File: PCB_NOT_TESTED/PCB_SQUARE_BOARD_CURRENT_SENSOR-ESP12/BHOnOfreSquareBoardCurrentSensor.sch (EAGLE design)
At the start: 26 parts, among them J6 8p, J7 8p, K1 OMRON-G3MB-202P-SSR2, K2 OMRON-G3MB-202P-SSR2, Q1 S8050, U2 esp12, X2 PLUG

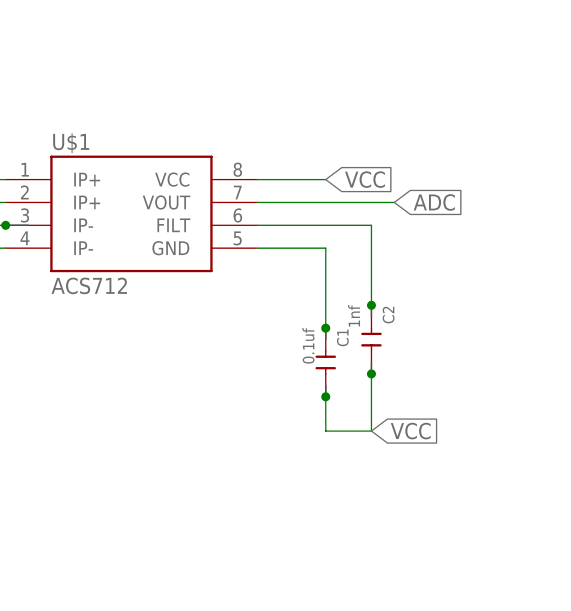
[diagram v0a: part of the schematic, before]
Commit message: REV1 teste OK demo em https://youtu.be/ygMf2j0tS-s
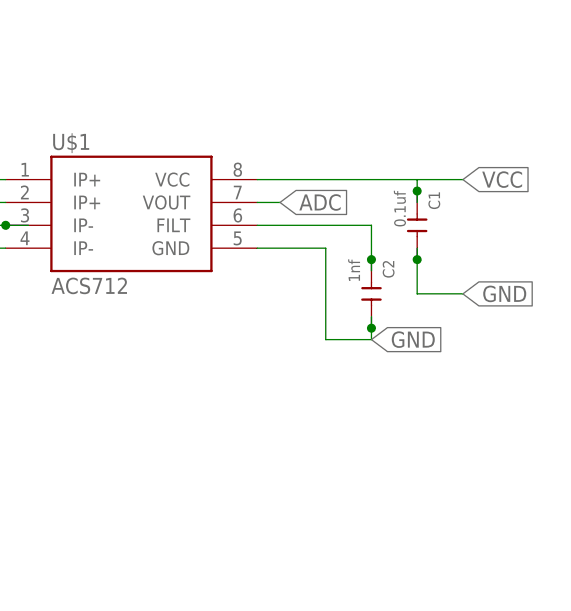
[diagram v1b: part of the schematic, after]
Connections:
- removed net N$3: C1.1, U$1.GND
- net GND: now also C1.2, C2.2, U$1.GND
- net VCC: now also C1.1; no longer C1.2, C2.2
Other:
- moved on the sheet: C1, C2
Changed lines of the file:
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@@
 <instance part="X2" gate="-4" x="2.54" y="10.16"/>
 <instance part="U$1" gate="G$1" x="218.44" y="66.04"/>
-<instance part="C1" gate="G$1" x="238.76" y="50.8" rot="R270"/>
-<instance part="C2" gate="G$1" x="243.84" y="53.34" rot="R270"/>
+<instance part="C1" gate="G$1" x="248.92" y="66.04" rot="R270"/>
+<instance part="C2" gate="G$1" x="243.84" y="58.42" rot="R270"/>
 </instances>
 <busses>
@@
 <label x="88.9" y="109.22" size="1.778" layer="95" xref="yes"/>
 </segment>
+<segment>
+<wire x1="248.92" y1="63.5" x2="248.92" y2="62.23" width="0.1524" layer="91"/>
+<wire x1="248.92" y1="62.23" x2="248.92" y2="58.42" width="0.1524" layer="91"/>
+<wire x1="248.92" y1="58.42" x2="254" y2="58.42" width="0.1524" layer="91"/>
+<label x="254" y="58.42" size="1.778" layer="95" xref="yes"/>
+<pinref part="C1" gate="G$1" pin="2"/>
+<junction x="248.92" y="62.23"/>
+</segment>
+<segment>
+<pinref part="U$1" gate="G$1" pin="GND"/>
+<wire x1="231.14" y1="63.5" x2="238.76" y2="63.5" width="0.1524" layer="91"/>
+<wire x1="238.76" y1="63.5" x2="238.76" y2="53.34" width="0.1524" layer="91"/>
+<wire x1="238.76" y1="53.34" x2="243.84" y2="53.34" width="0.1524" layer="91"/>
+<wire x1="243.84" y1="53.34" x2="243.84" y2="54.61" width="0.1524" layer="91"/>
+<pinref part="C2" gate="G$1" pin="2"/>
+<wire x1="243.84" y1="54.61" x2="243.84" y2="55.88" width="0.1524" layer="91"/>
+<junction x="243.84" y="54.61"/>
+<label x="243.84" y="53.34" size="1.778" layer="95" xref="yes"/>
+</segment>
 </net>
 <net name="VCC" class="0">
@@
 </segment>
 <segment>
-<label x="243.84" y="43.18" size="1.778" layer="95" xref="yes"/>
-<wire x1="238.76" y1="48.26" x2="238.76" y2="46.99" width="0.1524" layer="91"/>
-<wire x1="238.76" y1="46.99" x2="238.76" y2="43.18" width="0.1524" layer="91"/>
-<wire x1="238.76" y1="43.18" x2="243.84" y2="43.18" width="0.1524" layer="91"/>
-<wire x1="243.84" y1="43.18" x2="243.84" y2="49.53" width="0.1524" layer="91"/>
-<pinref part="C1" gate="G$1" pin="2"/>
-<junction x="238.76" y="46.99"/>
-<pinref part="C2" gate="G$1" pin="2"/>
-<wire x1="243.84" y1="49.53" x2="243.84" y2="50.8" width="0.1524" layer="91"/>
-<junction x="243.84" y="49.53"/>
-</segment>
-<segment>
 <pinref part="U$1" gate="G$1" pin="VCC"/>
-<wire x1="231.14" y1="71.12" x2="238.76" y2="71.12" width="0.1524" layer="91"/>
-<label x="238.76" y="71.12" size="1.778" layer="95" xref="yes"/>
+<wire x1="231.14" y1="71.12" x2="248.92" y2="71.12" width="0.1524" layer="91"/>
+<label x="254" y="71.12" size="1.778" layer="95" xref="yes"/>
+<wire x1="248.92" y1="71.12" x2="254" y2="71.12" width="0.1524" layer="91"/>
+<wire x1="248.92" y1="68.58" x2="248.92" y2="69.85" width="0.1524" layer="91"/>
+<pinref part="C1" gate="G$1" pin="1"/>
+<wire x1="248.92" y1="69.85" x2="248.92" y2="71.12" width="0.1524" layer="91"/>
+<junction x="248.92" y="69.85"/>
 </segment>
 </net>
@@
 <segment>
 <pinref part="U$1" gate="G$1" pin="VOUT"/>
-<wire x1="231.14" y1="68.58" x2="246.38" y2="68.58" width="0.1524" layer="91"/>
-<label x="246.38" y="68.58" size="1.778" layer="95" xref="yes"/>
+<wire x1="231.14" y1="68.58" x2="233.68" y2="68.58" width="0.1524" layer="91"/>
+<label x="233.68" y="68.58" size="1.778" layer="95" xref="yes"/>
 </segment>
 </net>
@@
 </segment>
 </net>
-<net name="N$3" class="0">
-<segment>
-<pinref part="U$1" gate="G$1" pin="GND"/>
-<wire x1="231.14" y1="63.5" x2="238.76" y2="63.5" width="0.1524" layer="91"/>
-<wire x1="238.76" y1="63.5" x2="238.76" y2="54.61" width="0.1524" layer="91"/>
-<pinref part="C1" gate="G$1" pin="1"/>
-<wire x1="238.76" y1="54.61" x2="238.76" y2="53.34" width="0.1524" layer="91"/>
-<junction x="238.76" y="54.61"/>
-</segment>
-</net>
 <net name="N$4" class="0">
 <segment>
 <pinref part="U$1" gate="G$1" pin="FILT"/>
 <wire x1="231.14" y1="66.04" x2="243.84" y2="66.04" width="0.1524" layer="91"/>
-<wire x1="243.84" y1="66.04" x2="243.84" y2="57.15" width="0.1524" layer="91"/>
+<wire x1="243.84" y1="60.96" x2="243.84" y2="62.23" width="0.1524" layer="91"/>
 <pinref part="C2" gate="G$1" pin="1"/>
-<wire x1="243.84" y1="57.15" x2="243.84" y2="55.88" width="0.1524" layer="91"/>
-<junction x="243.84" y="57.15"/>
-</segment>
-</net>
+<wire x1="243.84" y1="62.23" x2="243.84" y2="66.04" width="0.1524" layer="91"/>
+<junction x="243.84" y="62.23"/>
+</segment>
+</net>

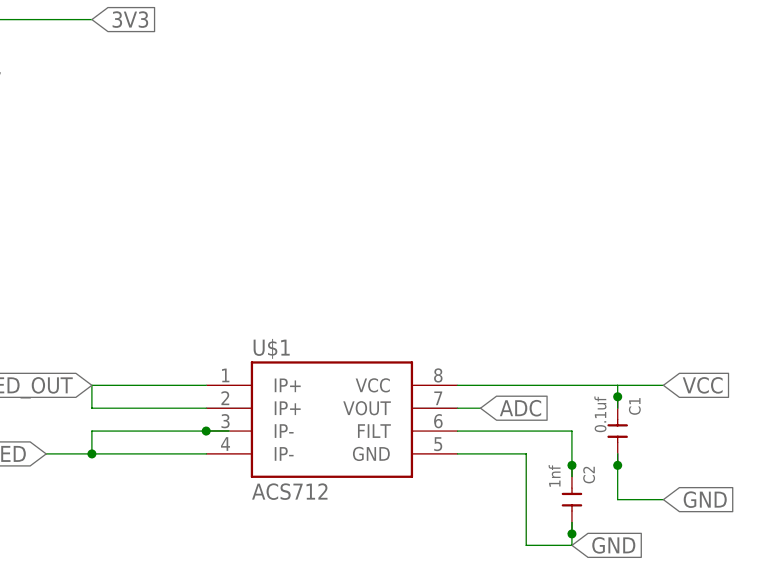
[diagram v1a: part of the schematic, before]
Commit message: change switch place
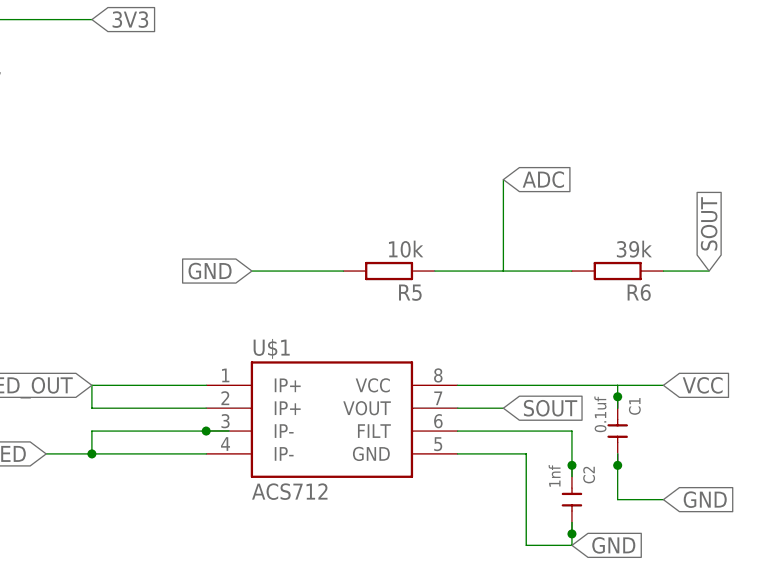
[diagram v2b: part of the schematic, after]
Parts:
- added R5: 10k, resistor:R-EU_R0603
- added R6: 39k, resistor:R-EU_R0603
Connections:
- new net SOUT: R6.1, U$1.VOUT
- net ADC: now also R5.1, R6.2; no longer U$1.VOUT
- net GND: now also R5.2
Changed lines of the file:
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@@
 <part name="C1" library="Seeed-Capacitor" library_urn="urn:adsk.eagle:library:464" deviceset="CERAMIC-100NF-50V-10%-X7R(0805)" device="" package3d_urn="urn:adsk.eagle:package:32459/1" value="0.1uf"/>
 <part name="C2" library="Seeed-Capacitor" library_urn="urn:adsk.eagle:library:464" deviceset="CERAMIC-100NF-50V-10%-X7R(0805)" device="" package3d_urn="urn:adsk.eagle:package:32459/1" value="1nf"/>
+<part name="R5" library="resistor" library_urn="urn:adsk.eagle:library:348" deviceset="R-EU_" device="R0603" package3d_urn="urn:adsk.eagle:package:26057/1" value="10k"/>
+<part name="R6" library="resistor" library_urn="urn:adsk.eagle:library:348" deviceset="R-EU_" device="R0603" package3d_urn="urn:adsk.eagle:package:26057/1" value="39k"/>
 </parts>
 <sheets>
@@
 <instance part="C1" gate="G$1" x="248.92" y="66.04" rot="R270"/>
 <instance part="C2" gate="G$1" x="243.84" y="58.42" rot="R270"/>
+<instance part="R5" gate="G$1" x="223.52" y="83.82" rot="R180"/>
+<instance part="R6" gate="G$1" x="248.92" y="83.82" rot="R180"/>
 </instances>
 <busses>
@@
 <label x="243.84" y="53.34" size="1.778" layer="95" xref="yes"/>
 </segment>
+<segment>
+<pinref part="R5" gate="G$1" pin="2"/>
+<wire x1="218.44" y1="83.82" x2="208.28" y2="83.82" width="0.1524" layer="91"/>
+<label x="208.28" y="83.82" size="1.778" layer="95" rot="R180" xref="yes"/>
+</segment>
 </net>
 <net name="VCC" class="0">
@@
 </segment>
 <segment>
-<pinref part="U$1" gate="G$1" pin="VOUT"/>
-<wire x1="231.14" y1="68.58" x2="233.68" y2="68.58" width="0.1524" layer="91"/>
-<label x="233.68" y="68.58" size="1.778" layer="95" xref="yes"/>
+<pinref part="R5" gate="G$1" pin="1"/>
+<wire x1="228.6" y1="83.82" x2="236.22" y2="83.82" width="0.1524" layer="91"/>
+<pinref part="R6" gate="G$1" pin="2"/>
+<wire x1="236.22" y1="83.82" x2="243.84" y2="83.82" width="0.1524" layer="91"/>
+<wire x1="236.22" y1="83.82" x2="236.22" y2="93.98" width="0.1524" layer="91"/>
+<label x="236.22" y="93.98" size="1.778" layer="95" xref="yes"/>
 </segment>
 </net>
@@
 </segment>
 </net>
+<net name="SOUT" class="0">
+<segment>
+<pinref part="U$1" gate="G$1" pin="VOUT"/>
+<wire x1="231.14" y1="68.58" x2="236.22" y2="68.58" width="0.1524" layer="91"/>
+<label x="236.22" y="68.58" size="1.778" layer="95" xref="yes"/>
+</segment>
+<segment>
+<pinref part="R6" gate="G$1" pin="1"/>
+<wire x1="254" y1="83.82" x2="259.08" y2="83.82" width="0.1524" layer="91"/>
+<label x="259.08" y="83.82" size="1.778" layer="95" rot="R90" xref="yes"/>
+</segment>
+</net>
